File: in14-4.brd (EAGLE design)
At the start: 160 x 39 mm, 15 parts, among them IC1 4094D, IC3 4094D, Q1 K155ID1, Q2 K155ID1, Q3 K155ID1, Q4 K155ID1

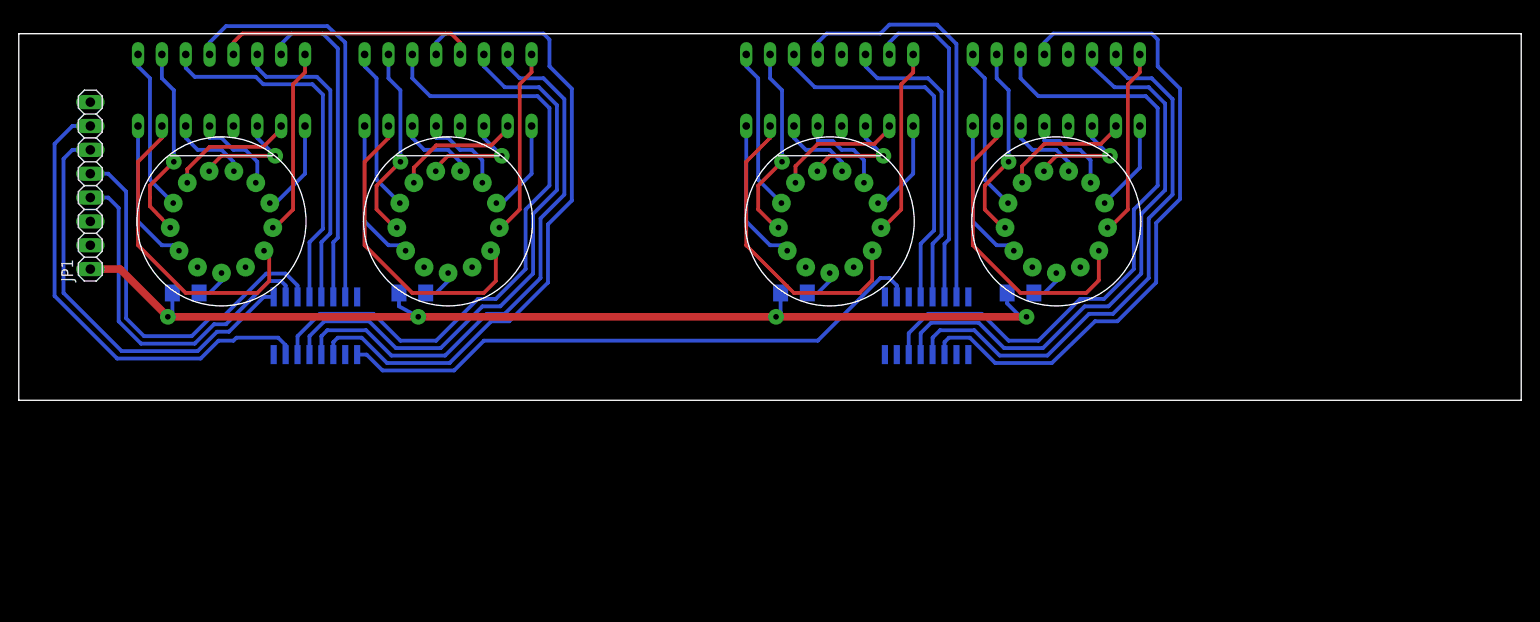
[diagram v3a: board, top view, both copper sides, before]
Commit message: Dimensions defined
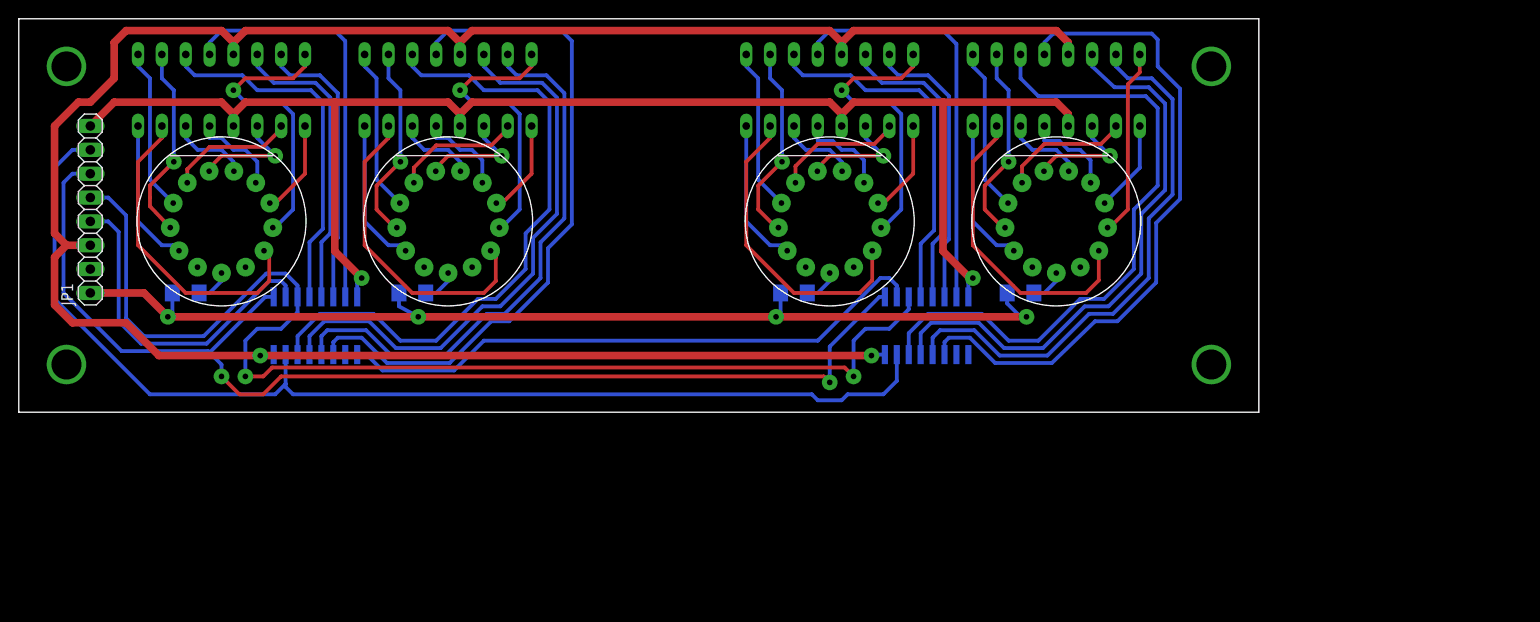
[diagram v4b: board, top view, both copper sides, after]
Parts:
- moved JP1 2.54 mm to (7.62, 41.9)
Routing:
- net +5V: track 27.5 -> 238.0 mm, vias 0 -> 2
- net GND: track 0.00 -> 158.5 mm, vias 0 -> 2
- net N$32: track 41.6 -> 129.3 mm, vias 0 -> 2
- net N$33: track 44.9 -> 124.0 mm, vias 0 -> 2
- net N$34: track 50.4 -> 120.6 mm
- net N$14: track 20.0 -> 30.5 mm, vias 0 -> 1
- net N$45: track 20.0 -> 30.5 mm, vias 0 -> 1
- net N$3: track 20.0 -> 30.5 mm, vias 0 -> 1
- net N$36: track 35.3 -> 30.5 mm
- net N$69: track 34.9 -> 30.4 mm
- net N$31: track 38.5 -> 35.9 mm
- net N$30: track 71.0 -> 72.5 mm
- net 200V: track 114.8 -> 113.8 mm
- net N$63: track 39.3 -> 38.8 mm
- net N$37: track 32.7 -> 32.2 mm
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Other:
- board size 160 x 39 mm -> 132.1 x 41.9 mm

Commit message: Update
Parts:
- moved R1 20.3 mm to (17.8, 12.7)
- moved R2 20.3 mm to (41.9, 12.7)
- moved R3 20.3 mm to (82.5, 12.7)
- moved R4 20.3 mm to (106.7, 12.7)
- moved IC1 20.3 mm to (96.7, 9.21)
- moved IC3 20.3 mm to (31.6, 9.21)
- moved Q1 20.3 mm to (21.6, 34.3)
- moved Q2 20.3 mm to (45.7, 34.3)
- moved Q3 20.3 mm to (86.4, 34.3)
- moved Q4 20.3 mm to (110.5, 34.3)
- moved UL1 20.3 mm to (21.6, 20.3)
- moved UL2 20.3 mm to (45.7, 20.3)
- moved UL3 20.3 mm to (86.4, 20.3)
- moved UL4 20.3 mm to (110.5, 20.3)
- moved JP1 20.3 mm to (7.62, 21.6)
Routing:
- net +5V: track 238.0 -> 253.2 mm
- net N$34: track 120.6 -> 129.4 mm
- net 200V: track 113.8 -> 119.0 mm
- net N$32: track 129.3 -> 133.8 mm
- net N$33: track 124.0 -> 128.2 mm
- net N$67: track 63.8 -> 65.9 mm
- net GND: track 158.5 -> 160.6 mm

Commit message: .
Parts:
- R1, R2, R3, R4: value 10K -> 10k; device rcl:R1206 -> SparkFun-Passives:1206
- moved R2 1.27 mm to (43.2, 12.7)
- moved R1 1.27 mm to (19.1, 12.7)
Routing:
- net N$22: track 3.76 -> 2.65 mm
- net N$11: track 3.76 -> 2.65 mm

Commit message: .
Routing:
- net N$57: track 9.75 -> 8.82 mm
- net N$47: track 9.75 -> 8.82 mm
- net N$42: track 70.6 -> 71.4 mm
- net N$68: track 44.0 -> 43.2 mm
- net N$35: track 44.1 -> 43.3 mm
- net N$5: track 9.70 -> 8.96 mm
- net N$16: track 9.57 -> 8.82 mm
- net N$30: track 72.5 -> 71.8 mm
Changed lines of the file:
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@@
 <wire x1="25.4" y1="26.67" x2="24.13" y2="27.94" width="0.4064" layer="16"/>
 <wire x1="24.13" y1="27.94" x2="22.86" y2="27.94" width="0.4064" layer="16"/>
-<wire x1="22.86" y1="27.94" x2="21.59" y2="29.21" width="0.4064" layer="16"/>
-<wire x1="21.59" y1="29.21" x2="20.32" y2="29.21" width="0.4064" layer="16"/>
-<wire x1="20.32" y1="29.21" x2="20.32" y2="30.48" width="0.4064" layer="16"/>
+<wire x1="22.86" y1="27.94" x2="20.32" y2="30.48" width="0.4064" layer="16"/>
 </signal>
 <signal name="N$6">
@@
 <wire x1="49.367175" y1="26.832825" x2="48.26" y2="27.94" width="0.4064" layer="16"/>
 <wire x1="48.26" y1="27.94" x2="46.99" y2="27.94" width="0.4064" layer="16"/>
-<wire x1="46.99" y1="27.94" x2="45.72" y2="29.21" width="0.4064" layer="16"/>
-<wire x1="45.72" y1="29.21" x2="44.45" y2="29.21" width="0.4064" layer="16"/>
-<wire x1="44.45" y1="29.21" x2="44.45" y2="30.48" width="0.4064" layer="16"/>
+<wire x1="46.99" y1="27.94" x2="44.45" y2="30.48" width="0.4064" layer="16"/>
 </signal>
 <signal name="N$17">
@@
 <wire x1="50.32375" y1="9.68375" x2="52.22875" y2="9.68375" width="0.4064" layer="16"/>
 <wire x1="52.22875" y1="9.68375" x2="58.89625" y2="16.35125" width="0.4064" layer="16"/>
-<wire x1="58.89625" y1="16.35125" x2="58.89625" y2="39.52875" width="0.4064" layer="16"/>
+<wire x1="58.89625" y1="16.35125" x2="58.89625" y2="38.25875" width="0.4064" layer="16"/>
 <contactref element="IC3" pad="11"/>
 <wire x1="33.49625" y1="6.1341" x2="33.49625" y2="7.46125" width="0.4064" layer="16"/>
-<wire x1="58.89625" y1="39.52875" x2="57.785" y2="40.64" width="0.4064" layer="16"/>
-<wire x1="57.785" y1="40.64" x2="45.72" y2="40.64" width="0.4064" layer="16"/>
+<wire x1="58.89625" y1="38.25875" x2="56.515" y2="40.64" width="0.4064" layer="16"/>
+<wire x1="56.515" y1="40.64" x2="45.72" y2="40.64" width="0.4064" layer="16"/>
 <wire x1="45.72" y1="40.64" x2="44.45" y2="39.37" width="0.4064" layer="16"/>
 <wire x1="44.45" y1="39.37" x2="44.45" y2="38.1" width="0.4064" layer="16"/>
@@
 <contactref element="Q3" pad="4"/>
 <contactref element="IC1" pad="7"/>
-<wire x1="99.85375" y1="12.2809" x2="99.85375" y2="39.21125" width="0.4064" layer="16"/>
-<wire x1="99.85375" y1="39.21125" x2="98.425" y2="40.64" width="0.4064" layer="16"/>
-<wire x1="98.425" y1="40.64" x2="86.36" y2="40.64" width="0.4064" layer="16"/>
+<wire x1="99.85375" y1="12.2809" x2="99.85375" y2="37.94125" width="0.4064" layer="16"/>
+<wire x1="99.85375" y1="37.94125" x2="97.155" y2="40.64" width="0.4064" layer="16"/>
+<wire x1="97.155" y1="40.64" x2="86.36" y2="40.64" width="0.4064" layer="16"/>
 <wire x1="86.36" y1="40.64" x2="85.09" y2="39.37" width="0.4064" layer="16"/>
 <wire x1="85.09" y1="39.37" x2="85.09" y2="38.1" width="0.4064" layer="16"/>
@@
 <wire x1="114.6175" y1="9.68375" x2="116.99875" y2="9.68375" width="0.4064" layer="16"/>
 <wire x1="116.99875" y1="9.68375" x2="123.66625" y2="16.35125" width="0.4064" layer="16"/>
-<wire x1="123.66625" y1="16.35125" x2="123.66625" y2="34.44875" width="0.4064" layer="16"/>
-<wire x1="123.66625" y1="34.44875" x2="121.285" y2="36.83" width="0.4064" layer="16"/>
-<wire x1="121.285" y1="36.83" x2="121.285" y2="39.6875" width="0.4064" layer="16"/>
-<wire x1="121.285" y1="39.6875" x2="120.65" y2="40.3225" width="0.4064" layer="16"/>
-<wire x1="120.65" y1="40.3225" x2="110.1725" y2="40.3225" width="0.4064" layer="16"/>
-<wire x1="110.1725" y1="40.3225" x2="109.22" y2="39.37" width="0.4064" layer="16"/>
+<wire x1="123.66625" y1="16.35125" x2="123.66625" y2="38.25875" width="0.4064" layer="16"/>
+<wire x1="110.49" y1="40.64" x2="109.22" y2="39.37" width="0.4064" layer="16"/>
 <wire x1="109.22" y1="39.37" x2="109.22" y2="38.1" width="0.4064" layer="16"/>
 <contactref element="IC1" pad="11"/>
 <wire x1="98.58375" y1="6.1341" x2="98.58375" y2="7.46125" width="0.4064" layer="16"/>
+<wire x1="123.66625" y1="38.25875" x2="121.285" y2="40.64" width="0.4064" layer="16"/>
+<wire x1="121.285" y1="40.64" x2="110.49" y2="40.64" width="0.4064" layer="16"/>
 </signal>
 <signal name="N$43">
@@
 <wire x1="90.007175" y1="26.832825" x2="88.9" y2="27.94" width="0.4064" layer="16"/>
 <wire x1="88.9" y1="27.94" x2="87.63" y2="27.94" width="0.4064" layer="16"/>
-<wire x1="87.63" y1="27.94" x2="86.6775" y2="28.8925" width="0.4064" layer="16"/>
-<wire x1="86.6775" y1="28.8925" x2="85.09" y2="28.8925" width="0.4064" layer="16"/>
-<wire x1="85.09" y1="28.8925" x2="85.09" y2="30.48" width="0.4064" layer="16"/>
+<wire x1="87.63" y1="27.94" x2="85.09" y2="30.48" width="0.4064" layer="16"/>
 </signal>
 <signal name="N$48">
@@
 <wire x1="114.137175" y1="26.832825" x2="113.03" y2="27.94" width="0.4064" layer="16"/>
 <wire x1="113.03" y1="27.94" x2="111.76" y2="27.94" width="0.4064" layer="16"/>
-<wire x1="111.76" y1="27.94" x2="110.8075" y2="28.8925" width="0.4064" layer="16"/>
-<wire x1="110.8075" y1="28.8925" x2="109.22" y2="28.8925" width="0.4064" layer="16"/>
-<wire x1="109.22" y1="28.8925" x2="109.22" y2="30.48" width="0.4064" layer="16"/>
+<wire x1="111.76" y1="27.94" x2="109.22" y2="30.48" width="0.4064" layer="16"/>
 </signal>
 <signal name="N$58">
@@
 <contactref element="Q1" pad="4"/>
 <contactref element="IC3" pad="7"/>
-<wire x1="34.76625" y1="12.2809" x2="34.76625" y2="39.52875" width="0.4064" layer="16"/>
-<wire x1="34.76625" y1="39.52875" x2="33.655" y2="40.64" width="0.4064" layer="16"/>
-<wire x1="33.655" y1="40.64" x2="21.59" y2="40.64" width="0.4064" layer="16"/>
+<wire x1="34.76625" y1="12.2809" x2="34.76625" y2="38.25875" width="0.4064" layer="16"/>
+<wire x1="34.76625" y1="38.25875" x2="32.385" y2="40.64" width="0.4064" layer="16"/>
+<wire x1="32.385" y1="40.64" x2="21.59" y2="40.64" width="0.4064" layer="16"/>
 <wire x1="21.59" y1="40.64" x2="20.32" y2="39.37" width="0.4064" layer="16"/>
 <wire x1="20.32" y1="39.37" x2="20.32" y2="38.1" width="0.4064" layer="16"/>
